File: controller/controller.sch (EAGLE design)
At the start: 26 parts, among them IC1 ATtiny25, IC2 74HC595N

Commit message: Routing erster Versuch
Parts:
- removed JP1: DISABLE, jumper:JP1Q
- removed R10: (no value), resistor:R-EU_0617/5V
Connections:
- removed net N$13: LED6.C, R7.2
- removed net N$14: LED5.C, R6.2
- removed net N$16: LED8.C, R9.2
- removed net N$17: LED7.C, R8.2
- removed net N$4: IC2A.G, JP1.1, R10.1
- new net N$11: LED7.A, R8.1
- new net N$12: LED8.A, R9.1
- new net N$5: LED1.A, R2.1
- new net N$8: LED4.A, R5.1
- net GND: now also IC2A.G, LED1.C, LED2.C, LED3.C, LED4.C, LED5.C, LED6.C, LED7.C, LED8.C; no longer R10.2, R2.1, R3.1, R4.1, R5.1, R6.1, R7.1, R8.1, R9.1
- net N$10: now also LED6.A, R7.1; no longer LED3.C, R4.2
- net N$6: now also LED2.A, R3.1; no longer LED2.C, R3.2
- net N$7: now also LED3.A, R4.1; no longer LED1.C, R2.2
- net N$9: now also LED5.A, R6.1; no longer LED4.C, R5.2
- net QA: now also R2.2; no longer LED1.A
- net QB: now also R3.2, X1-6.M; no longer LED2.A, X1-2.M
- net QC: now also R4.2, X1-2.M; no longer LED3.A, X1-3.M
- net QD: now also R5.2; no longer LED4.A, X1-4.M
- net QE: now also R6.2; no longer LED5.A, X1-6.M
- net QF: now also R7.2; no longer LED6.A, X1-7.M
- net QG: now also R8.2; no longer LED7.A, X1-8.M
- net QH: now also R9.2; no longer LED8.A, X1-9.M
- net VCC: no longer JP1.2
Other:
- moved on the sheet: LED1, LED2, LED3, LED4, LED5, LED6, LED7, LED8, R2, R3, R4, R5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

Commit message: PLatinenlayout fertig
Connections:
- removed net N$1: SV2.3, SV3.3
- net MISO: now also SV2.3, SV3.3; no longer IC2A.SER
- net N$2: now also IC2A.SER; no longer IC2A.RCK
- net N$3: now also IC2A.RCK
- net QB: now also R6.2; no longer R3.2
- net QC: now also R3.2; no longer R4.2
- net QD: now also R7.2, X1-7.M; no longer R5.2
- net QE: now also R4.2, X1-3.M; no longer R6.2
- net QF: now also R8.2, X1-8.M; no longer R7.2
- net QG: now also R5.2, X1-4.M; no longer R8.2
- net QH: now also X1-9.M
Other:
- moved on the sheet: LED1, LED2, LED3, LED4, LED5, LED6, LED7, LED8, R2, R3, R4, R5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

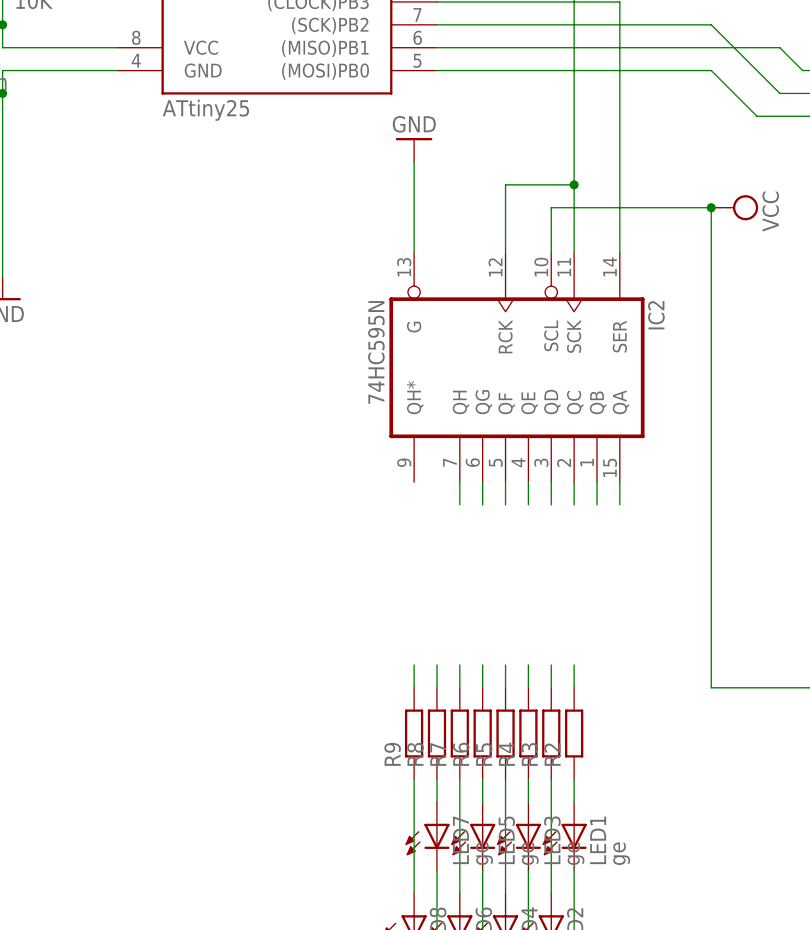
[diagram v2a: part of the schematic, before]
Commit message: Jumper zum Board hinzugefügt
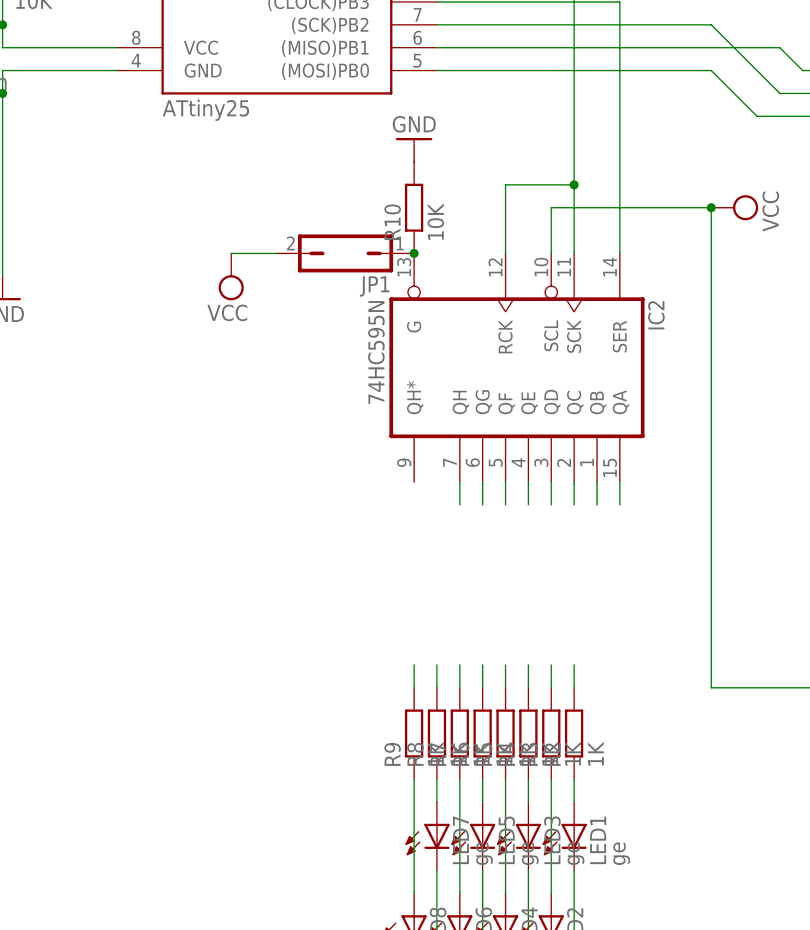
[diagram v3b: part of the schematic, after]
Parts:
- added JP1: (no value), jumper:JP1Q
- added R10: 10K, resistor:R-EU_0207/7
- R2, R3, R4, R5, R6, R7, R8, R9: value (none) -> 1K
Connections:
- new net REG_DISABLE: IC2A.G, JP1.1, R10.1
- net GND: now also R10.2; no longer IC2A.G
- net VCC: now also JP1.2
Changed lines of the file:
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@@
 <part name="LED1" library="led" deviceset="LED" device="5MM" value="ge"/>
 <part name="LED2" library="led" deviceset="LED" device="5MM" value="rt"/>
-<part name="R2" library="resistor" deviceset="R-EU_" device="0309/12"/>
-<part name="R3" library="resistor" deviceset="R-EU_" device="0309/12"/>
+<part name="R2" library="resistor" deviceset="R-EU_" device="0309/12" value="1K"/>
+<part name="R3" library="resistor" deviceset="R-EU_" device="0309/12" value="1K"/>
 <part name="LED3" library="led" deviceset="LED" device="5MM" value="ge"/>
 <part name="LED4" library="led" deviceset="LED" device="5MM" value="rt"/>
-<part name="R4" library="resistor" deviceset="R-EU_" device="0309/12"/>
-<part name="R5" library="resistor" deviceset="R-EU_" device="0309/12"/>
+<part name="R4" library="resistor" deviceset="R-EU_" device="0309/12" value="1K"/>
+<part name="R5" library="resistor" deviceset="R-EU_" device="0309/12" value="1K"/>
 <part name="LED5" library="led" deviceset="LED" device="5MM" value="ge"/>
 <part name="LED6" library="led" deviceset="LED" device="5MM" value="rt"/>
-<part name="R6" library="resistor" deviceset="R-EU_" device="0309/12"/>
-<part name="R7" library="resistor" deviceset="R-EU_" device="0309/12"/>
+<part name="R6" library="resistor" deviceset="R-EU_" device="0309/12" value="1K"/>
+<part name="R7" library="resistor" deviceset="R-EU_" device="0309/12" value="1K"/>
 <part name="LED7" library="led" deviceset="LED" device="5MM" value="ge"/>
 <part name="LED8" library="led" deviceset="LED" device="5MM" value="rt"/>
-<part name="R8" library="resistor" deviceset="R-EU_" device="0309/12"/>
-<part name="R9" library="resistor" deviceset="R-EU_" device="0309/12"/>
+<part name="R8" library="resistor" deviceset="R-EU_" device="0309/12" value="1K"/>
+<part name="R9" library="resistor" deviceset="R-EU_" device="0309/12" value="1K"/>
 <part name="GND6" library="supply1" deviceset="GND" device=""/>
 <part name="X1" library="con-subd" deviceset="M09HPS" device=""/>
 <part name="GND7" library="supply1" deviceset="GND" device=""/>
+<part name="R10" library="resistor" deviceset="R-EU_" device="0207/7" value="10K"/>
+<part name="JP1" library="jumper" deviceset="JP1Q" device=""/>
+<part name="SUPPLY6" library="supply2" deviceset="VCC" device=""/>
 </parts>
 <sheets>
@@
 <instance part="X1" gate="-1" x="83.82" y="-33.02"/>
 <instance part="GND7" gate="1" x="81.28" y="-60.96"/>
+<instance part="R10" gate="G$1" x="25.4" y="10.16" rot="R90"/>
+<instance part="JP1" gate="A" x="17.78" y="5.08" rot="R90"/>
+<instance part="SUPPLY6" gate="G$1" x="5.08" y="2.54" rot="R180"/>
 </instances>
 <busses>
@@
 <wire x1="58.42" y1="-43.18" x2="58.42" y2="10.16" width="0.1524" layer="91"/>
 <junction x="58.42" y="10.16"/>
+</segment>
+<segment>
+<pinref part="JP1" gate="A" pin="2"/>
+<pinref part="SUPPLY6" gate="G$1" pin="VCC"/>
+<wire x1="10.16" y1="5.08" x2="5.08" y2="5.08" width="0.1524" layer="91"/>
 </segment>
 </net>
@@
 </segment>
 <segment>
-<pinref part="GND5" gate="1" pin="GND"/>
-<pinref part="IC2" gate="A" pin="G"/>
-<wire x1="25.4" y1="15.24" x2="25.4" y2="5.08" width="0.1524" layer="91"/>
-</segment>
-<segment>
 <pinref part="X1" gate="-G" pin="G1"/>
 <wire x1="81.28" y1="-58.42" x2="81.28" y2="-55.88" width="0.1524" layer="91"/>
@@
 <pinref part="GND7" gate="1" pin="GND"/>
 <junction x="81.28" y="-58.42"/>
+</segment>
+<segment>
+<pinref part="GND5" gate="1" pin="GND"/>
+<pinref part="R10" gate="G$1" pin="2"/>
 </segment>
 </net>
@@
 </segment>
 </net>
+<net name="REG_DISABLE" class="0">
+<segment>
+<pinref part="IC2" gate="A" pin="G"/>
+<pinref part="R10" gate="G$1" pin="1"/>
+<pinref part="JP1" gate="A" pin="1"/>
+<junction x="25.4" y="5.08"/>
+<pinref part="JP1" gate="A" pin="1"/>
+</segment>
+</net>

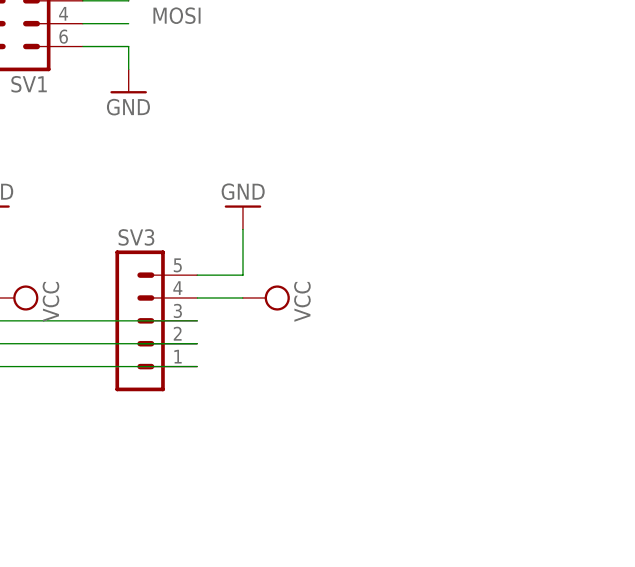
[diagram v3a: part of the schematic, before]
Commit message: * Platinenlayout nochmal angepasst (hauptsächlich Leiterbahndicken) * dritten Bus-Stecker vorgesehen
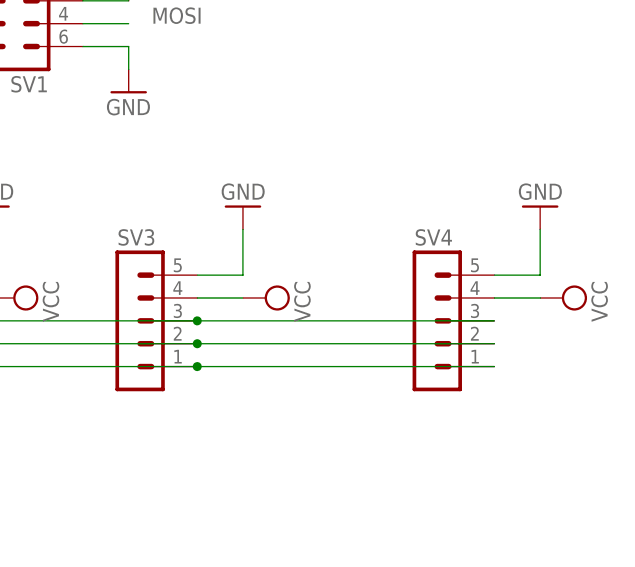
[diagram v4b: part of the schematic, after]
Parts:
- added SV4: (no value), con-lstb:MA05-1
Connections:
- net GND: now also SV4.5
- net MISO: now also SV4.3
- net MOSI: now also SV4.1
- net SCK: now also SV4.2
- net VCC: now also SV4.4
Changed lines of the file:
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@@
 <part name="JP1" library="jumper" deviceset="JP1Q" device=""/>
 <part name="SUPPLY6" library="supply2" deviceset="VCC" device=""/>
+<part name="SV4" library="con-lstb" deviceset="MA05-1" device=""/>
+<part name="GND8" library="supply1" deviceset="GND" device=""/>
+<part name="SUPPLY7" library="supply2" deviceset="VCC" device=""/>
 </parts>
 <sheets>
@@
 <instance part="JP1" gate="A" x="17.78" y="5.08" rot="R90"/>
 <instance part="SUPPLY6" gate="G$1" x="5.08" y="2.54" rot="R180"/>
+<instance part="SV4" gate="G$1" x="132.08" y="25.4"/>
+<instance part="GND8" gate="1" x="144.78" y="38.1" rot="R180"/>
+<instance part="SUPPLY7" gate="G$1" x="147.32" y="27.94" rot="R270"/>
 </instances>
 <busses>
@@
 <pinref part="SUPPLY6" gate="G$1" pin="VCC"/>
 <wire x1="10.16" y1="5.08" x2="5.08" y2="5.08" width="0.1524" layer="91"/>
+</segment>
+<segment>
+<pinref part="SUPPLY7" gate="G$1" pin="VCC"/>
+<pinref part="SV4" gate="G$1" pin="4"/>
+<wire x1="144.78" y1="27.94" x2="139.7" y2="27.94" width="0.1524" layer="91"/>
 </segment>
 </net>
@@
 <pinref part="R10" gate="G$1" pin="2"/>
 </segment>
+<segment>
+<pinref part="GND8" gate="1" pin="GND"/>
+<wire x1="144.78" y1="35.56" x2="144.78" y2="30.48" width="0.1524" layer="91"/>
+<pinref part="SV4" gate="G$1" pin="5"/>
+<wire x1="144.78" y1="30.48" x2="139.7" y2="30.48" width="0.1524" layer="91"/>
+</segment>
 </net>
 <net name="RESET" class="0">
@@
 </segment>
 <segment>
+<pinref part="SV4" gate="G$1" pin="3"/>
+<wire x1="106.68" y1="25.4" x2="139.7" y2="25.4" width="0.1524" layer="91"/>
 <pinref part="SV2" gate="G$1" pin="3"/>
 <pinref part="SV3" gate="G$1" pin="3"/>
@@
 <wire x1="68.58" y1="25.4" x2="78.74" y2="25.4" width="0.1524" layer="91"/>
 <junction x="78.74" y="25.4"/>
+<junction x="106.68" y="25.4"/>
 </segment>
 </net>
@@
 </segment>
 <segment>
+<pinref part="SV4" gate="G$1" pin="2"/>
+<wire x1="106.68" y1="22.86" x2="139.7" y2="22.86" width="0.1524" layer="91"/>
 <pinref part="IC1" gate="G$1" pin="(SCK)PB2"/>
 <wire x1="27.94" y1="30.48" x2="58.42" y2="30.48" width="0.1524" layer="91"/>
@@
 <wire x1="78.74" y1="22.86" x2="106.68" y2="22.86" width="0.1524" layer="91"/>
 <junction x="78.74" y="22.86"/>
+<junction x="106.68" y="22.86"/>
 </segment>
 </net>
@@
 </segment>
 <segment>
+<pinref part="SV4" gate="G$1" pin="1"/>
+<wire x1="106.68" y1="20.32" x2="139.7" y2="20.32" width="0.1524" layer="91"/>
 <pinref part="IC1" gate="G$1" pin="(MOSI)PB0"/>
 <wire x1="27.94" y1="25.4" x2="58.42" y2="25.4" width="0.1524" layer="91"/>
@@
 <wire x1="78.74" y1="20.32" x2="106.68" y2="20.32" width="0.1524" layer="91"/>
 <junction x="78.74" y="20.32"/>
-</segment>
-</net>
+<junction x="106.68" y="20.32"/>
+</segment>
+</net>
